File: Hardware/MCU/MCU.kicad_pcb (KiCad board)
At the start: 4 copper layers, 75 x 80 mm, 36 parts, among them U1 ESP32-S3-WROOM-1, U2 USBLC6-2P6

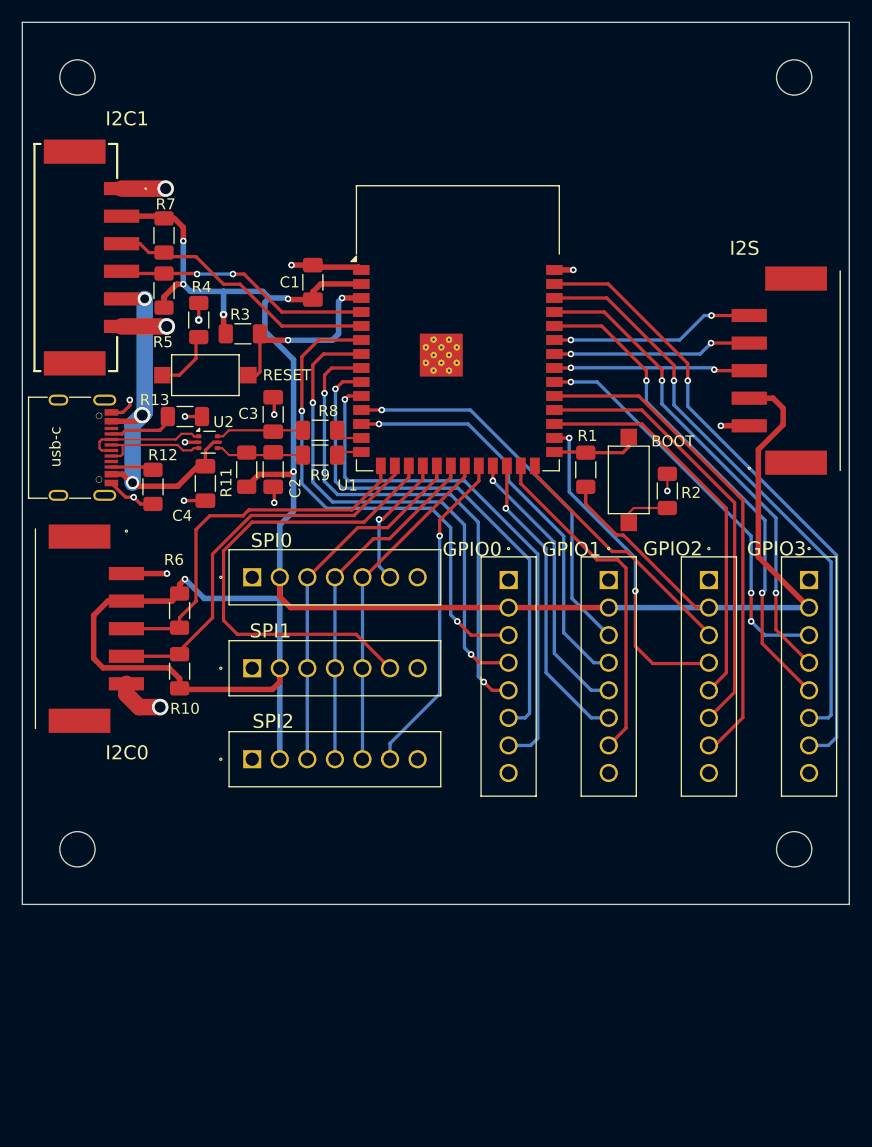
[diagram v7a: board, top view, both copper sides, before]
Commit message: boot en reset pin configuratie veranderd, pull up veranderd en capcitoren toegevoegd
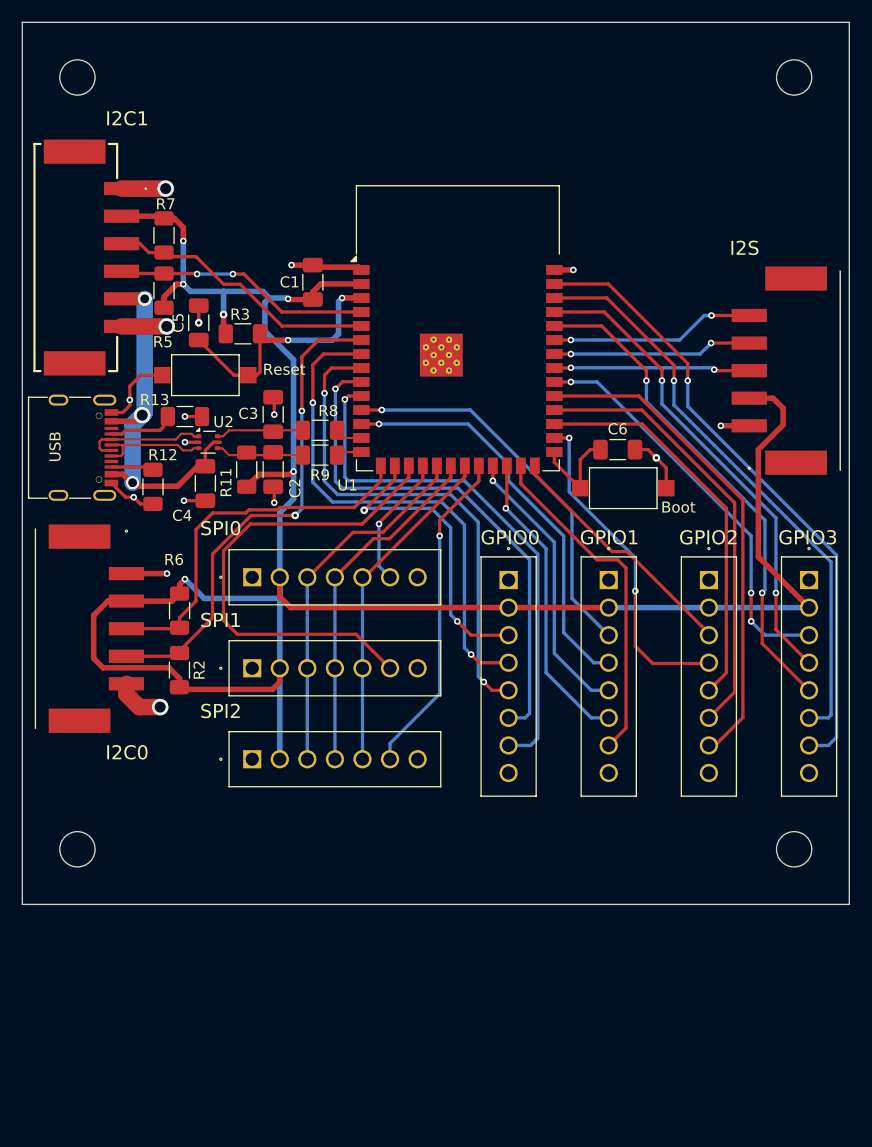
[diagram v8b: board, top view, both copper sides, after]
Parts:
- removed R1: 10k, Resistor_SMD:R_1206_3216Metric_Pad1.30x1.75mm_HandSolder
- removed R10: 4k7, Resistor_SMD:R_1206_3216Metric_Pad1.30x1.75mm_HandSolder
- removed R4: 470, Resistor_SMD:R_1206_3216Metric_Pad1.30x1.75mm_HandSolder
- added C5: 1u, Capacitor_SMD:C_1206_3216Metric_Pad1.33x1.80mm_HandSolder, F.Cu at (112.0, 76.2)
- added C6: 1u, Capacitor_SMD:C_1206_3216Metric_Pad1.33x1.80mm_HandSolder, F.Cu at (150.0, 87.8)
- R2: value 470 -> 4k7
- moved R2 47.1 mm to (110.2, 107.8), turned to -90 degrees
- moved Boot 0.90 mm to (150.5, 91.2), turned to 0 degrees
- renumbered BOOT to Boot, RESET to Reset, usb-c to USB
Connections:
- Boot pad 2: Net-(R2-Pad1) -> GND
- GPIO0 pad 3: io6 -> io46
- R2 pad 1: Net-(R2-Pad1) -> scl0
- R2 pad 2: GND -> +3.3V
- Reset pad 2: Net-(R4-Pad1) -> GND
- U1 pad 16: scl0 -> io46
- U1 pad 6: io6 -> scl0
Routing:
- net io6: track 46.6 -> 0.00 mm, vias 2 -> 0
- net io46: track 0.00 -> 27.7 mm, vias 0 -> 2
- net +3.3V: track 221.0 -> 204.3 mm
- net scl0: track 35.5 -> 44.8 mm, vias 0 -> 2
- net GND: track 36.4 -> 44.8 mm
- net Net-(R4-Pad1): track 5.72 -> 0.00 mm
- net reset: track 17.5 -> 23.2 mm
- net Net-(R2-Pad1): track 4.59 -> 0.00 mm
- net boot0: track 7.89 -> 9.06 mm
